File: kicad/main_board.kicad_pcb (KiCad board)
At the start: 2 copper layers, 42 x 67 mm, 66 parts, among them J1 Conn_01x18, J2 Conn_01x18, J3 Conn_01x07, J4 Conn_01x07, J5 Conn_01x07, J6 Conn_01x07, J7 Conn_01x07, J8 TYPE-C-31-M-12, J9 TYPE-C-31-M-12, Q1 DMG2301L-7, Q2 DMG2301L-7, Q3 DMG2301L-7, Q4 DMG2301L-7, Q5 DMG2301L-7, SW1 Reset, SW2 Boot, U1 XC6220B331MR, U2 RP2040, U3 W25Q128JVS, U4 COS724, U5 COS724, U6 USBLC6-2SC6, U7 USBLC6-2SC6, Y1 Crystal_GND24

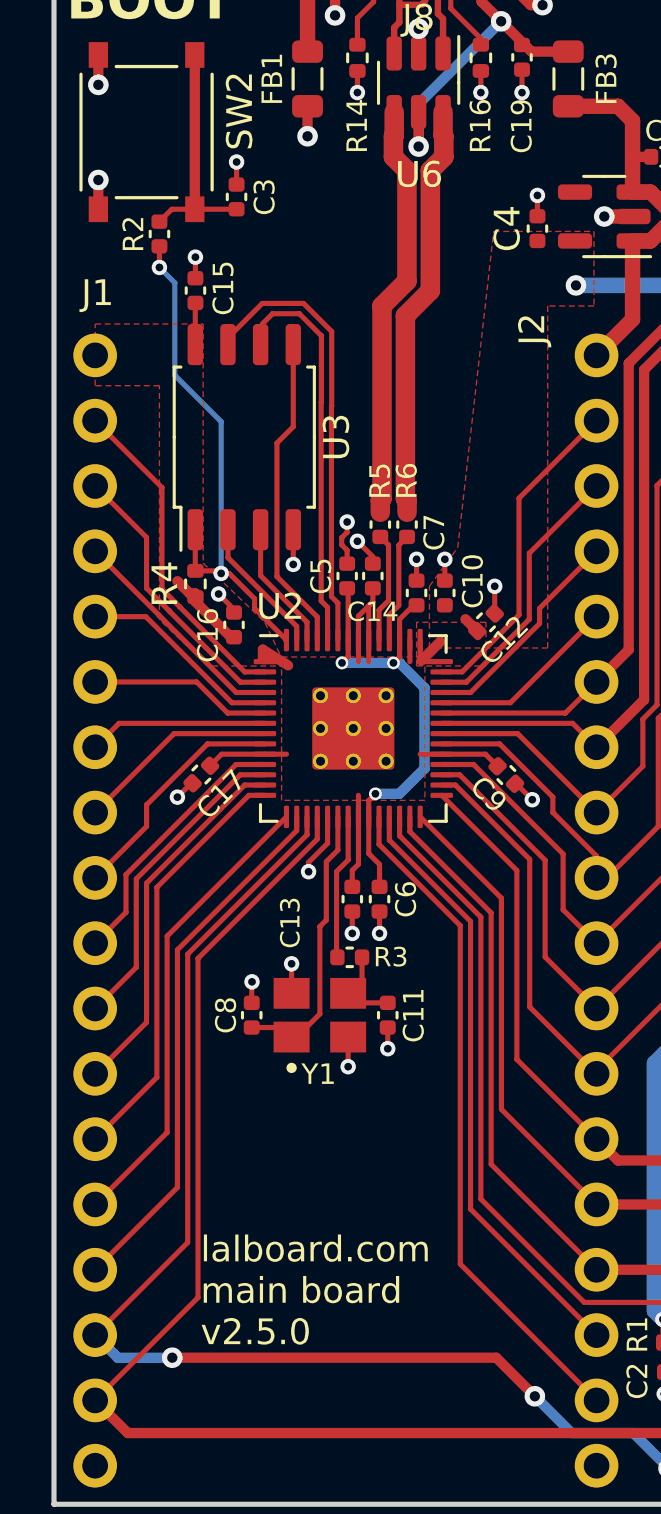
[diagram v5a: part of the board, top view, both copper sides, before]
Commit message: Main board v2.5.1
- Remove the decoupling capacitor on the boot selection button
- Fix the part selection in the BOM for the 27 ohm usb series resistors
(old part was mistakenly a 27kohm resistor)
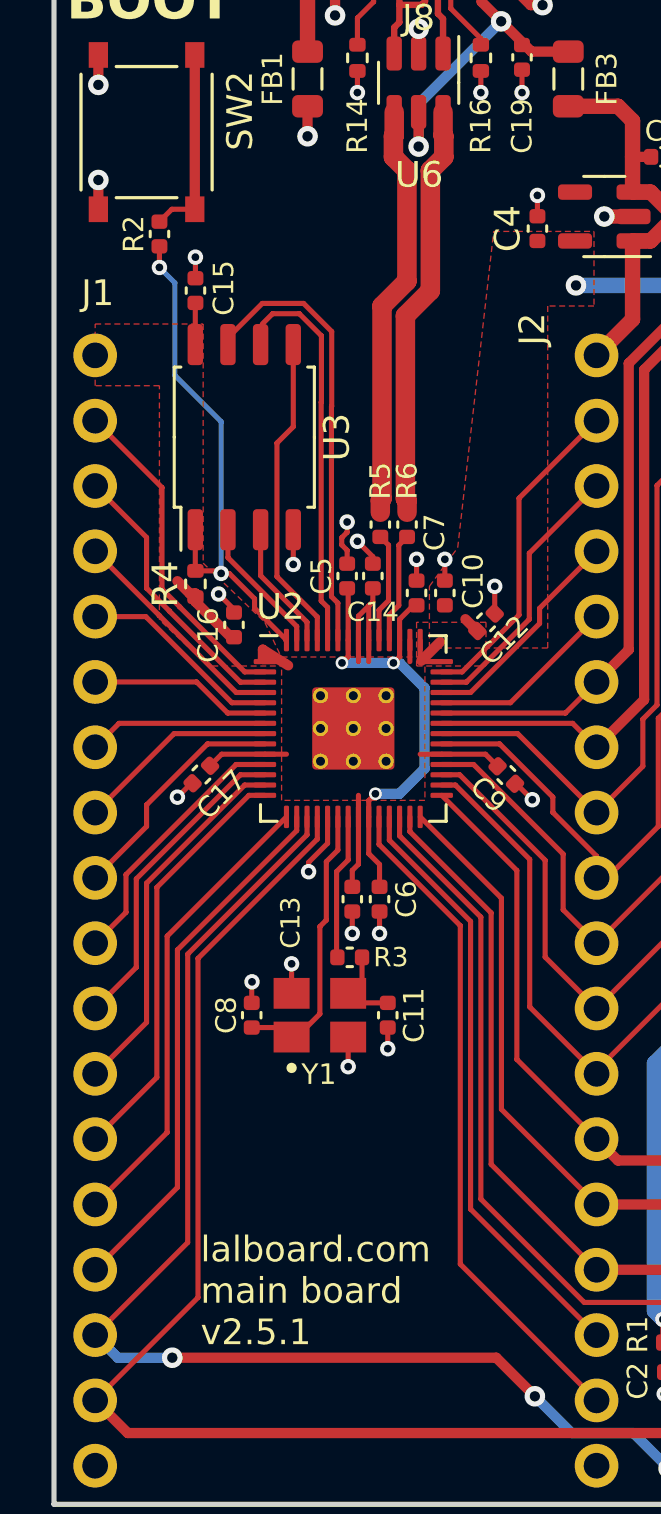
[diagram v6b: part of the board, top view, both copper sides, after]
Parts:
- removed C3: 100n, Capacitor_SMD:C_0402_1005Metric
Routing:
- net Net-(R2-Pad1): track 9.20 -> 7.57 mm
- net GND: track 50.4 -> 49.5 mm, vias 43 -> 42
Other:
- board text added: "lalboard.com main board v2.5.1"
- board text removed: "lalboard.com main board v2.5.0"
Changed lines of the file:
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@@
   (net 1 "GND")
   (net 2 "/RUN")
-  (net 3 "Net-(C3-Pad1)")
+  (net 3 "Net-(R2-Pad1)")
   (net 4 "+5V")
   (net 5 "Net-(U6-VBUS)")
@@
       (stroke (width 0.127) (type solid)) (layer "F.Fab"))
     (pad "1" smd rect (at -3 -1.875 270) (size 1 0.75) (layers "F.Cu" "F.Paste" "F.Mask")
-      (net 3 "Net-(C3-Pad1)") (pinfunction "1") (pintype "passive") (solder_mask_margin 0.102))
+      (net 3 "Net-(R2-Pad1)") (pinfunction "1") (pintype "passive") (solder_mask_margin 0.102))
     (pad "1" smd rect (at 3 -1.875 270) (size 1 0.75) (layers "F.Cu" "F.Paste" "F.Mask")
-      (net 3 "Net-(C3-Pad1)") (pinfunction "1") (pintype "passive") (solder_mask_margin 0.102))
+      (net 3 "Net-(R2-Pad1)") (pinfunction "1") (pintype "passive") (solder_mask_margin 0.102))
     (pad "2" smd rect (at -3 1.875 270) (size 1 0.75) (layers "F.Cu" "F.Paste" "F.Mask")
       (net 1 "GND") (pinfunction "2") (pintype "passive") (solder_mask_margin 0.102))
@@
     )
   )
-  (footprint "Capacitor_SMD:C_0402_1005Metric" (layer "F.Cu")
-    (at 157.1 49.1575 90)
-    (descr "Capacitor SMD 0402 (1005 Metric), square (rectangular) end terminal, IPC_7351 nominal, (Body size source: IPC-SM-782 page 76, https://www.pcb-3d.com/wordpress/wp-content/uploads/ipc-sm-782a_amendment_1_and_2.pdf), generated with kicad-footprint-generator")
-    (tags "capacitor")
-    (property "JLCPCB P/N" "C307331")
-    (property "Sheetfile" "main_board.kicad_sch")
-    (property "Sheetname" "")
-    (property "ki_description" "Unpolarized capacitor, small symbol")
-    (property "ki_keywords" "capacitor cap")
-    (attr smd)
-    (fp_text reference "C3" (at -0.000001 1.1 90) (layer "F.SilkS")
-        (effects (font (size 0.8 0.8) (thickness 0.15)))
-    )
-    (fp_text value "100n" (at 0 1.16 90) (layer "F.Fab")
-        (effects (font (size 1 1) (thickness 0.15)))
-    )
-    (fp_text user "${REFERENCE}" (at 0 0 90) (layer "F.Fab")
-        (effects (font (size 0.25 0.25) (thickness 0.04)))
-    )
-    (fp_line (start -0.107836 -0.36) (end 0.107836 -0.36)
-      (stroke (width 0.12) (type solid)) (layer "F.SilkS"))
-    (fp_line (start -0.107836 0.36) (end 0.107836 0.36)
-      (stroke (width 0.12) (type solid)) (layer "F.SilkS"))
-    (fp_line (start -0.91 -0.46) (end 0.91 -0.46)
-      (stroke (width 0.05) (type solid)) (layer "F.CrtYd"))
-    (fp_line (start -0.91 0.46) (end -0.91 -0.46)
-      (stroke (width 0.05) (type solid)) (layer "F.CrtYd"))
-    (fp_line (start 0.91 -0.46) (end 0.91 0.46)
-      (stroke (width 0.05) (type solid)) (layer "F.CrtYd"))
-    (fp_line (start 0.91 0.46) (end -0.91 0.46)
-      (stroke (width 0.05) (type solid)) (layer "F.CrtYd"))
-    (fp_line (start -0.5 -0.25) (end 0.5 -0.25)
-      (stroke (width 0.1) (type solid)) (layer "F.Fab"))
-    (fp_line (start -0.5 0.25) (end -0.5 -0.25)
-      (stroke (width 0.1) (type solid)) (layer "F.Fab"))
-    (fp_line (start 0.5 -0.25) (end 0.5 0.25)
-      (stroke (width 0.1) (type solid)) (layer "F.Fab"))
-    (fp_line (start 0.5 0.25) (end -0.5 0.25)
-      (stroke (width 0.1) (type solid)) (layer "F.Fab"))
-    (pad "1" smd roundrect (at -0.48 0 90) (size 0.56 0.62) (layers "F.Cu" "F.Paste" "F.Mask") (roundrect_rratio 0.25)
-      (net 3 "Net-(C3-Pad1)") (pintype "passive"))
-    (pad "2" smd roundrect (at 0.48 0 90) (size 0.56 0.62) (layers "F.Cu" "F.Paste" "F.Mask") (roundrect_rratio 0.25)
-      (net 1 "GND") (pintype "passive"))
-    (model "${KICAD6_3DMODEL_DIR}/Capacitor_SMD.3dshapes/C_0402_1005Metric.wrl"
-      (offset (xyz 0 0 0))
-      (scale (xyz 1 1 1))
-      (rotate (xyz 0 0 0))
-    )
-  )
   (footprint "Resistor_SMD:R_0402_1005Metric" (layer "F.Cu")
     (at 175.2 81.9425 -90)
@@
       (stroke (width 0.1) (type solid)) (layer "F.Fab"))
     (pad "1" smd roundrect (at -0.48 0 270) (size 0.56 0.62) (layers "F.Cu" "F.Paste" "F.Mask") (roundrect_rratio 0.25)
-      (net 3 "Net-(C3-Pad1)") (pintype "passive"))
+      (net 3 "Net-(R2-Pad1)") (pintype "passive"))
     (pad "2" smd roundrect (at 0.48 0 270) (size 0.56 0.62) (layers "F.Cu" "F.Paste" "F.Mask") (roundrect_rratio 0.25)
       (net 57 "/QSPI_SS") (pintype "passive"))
@@
     (property "Sheetfile" "main_board.kicad_sch")
     (property "Sheetname" "")
+    (property "exclude_from_bom" "")
     (property "ki_description" "Generic connector, single row, 01x07, script generated (kicad-library-utils/schlib/autogen/connector/)")
     (property "ki_keywords" "connector")
-    (attr through_hole)
+    (attr through_hole exclude_from_bom)
     (fp_text reference "J3" (at 4.5 2.81) (layer "F.SilkS")
         (effects (font (size 0.75 0.75) (thickness 0.15)))
@@
     (property "Sheetfile" "main_board.kicad_sch")
     (property "Sheetname" "")
+    (property "exclude_from_bom" "")
     (property "ki_description" "Generic connector, single row, 01x18, script generated (kicad-library-utils/schlib/autogen/connector/)")
     (property "ki_keywords" "connector")
-    (attr through_hole)
+    (attr through_hole exclude_from_bom)
     (fp_text reference "J1" (at 0.1 -2.42 180) (layer "F.SilkS")
         (effects (font (size 1 1) (thickness 0.15)))
@@
     (property "Sheetfile" "main_board.kicad_sch")
     (property "Sheetname" "")
+    (property "exclude_from_bom" "")
     (property "ki_description" "Generic connector, single row, 01x07, script generated (kicad-library-utils/schlib/autogen/connector/)")
     (property "ki_keywords" "connector")
-    (attr through_hole)
+    (attr through_hole exclude_from_bom)
     (fp_text reference "J7" (at 4.67 2.8) (layer "F.SilkS")
         (effects (font (size 0.75 0.75) (thickness 0.15)))
@@
     (property "Sheetfile" "main_board.kicad_sch")
     (property "Sheetname" "")
+    (property "exclude_from_bom" "")
     (property "ki_description" "Generic connector, single row, 01x07, script generated (kicad-library-utils/schlib/autogen/connector/)")
     (property "ki_keywords" "connector")
-    (attr through_hole)
+    (attr through_hole exclude_from_bom)
     (fp_text reference "J5" (at 4.5 2.8) (layer "F.SilkS")
         (effects (font (size 0.75 0.75) (thickness 0.15)))
@@
     (property "Sheetfile" "main_board.kicad_sch")
     (property "Sheetname" "")
+    (property "exclude_from_bom" "")
     (property "ki_description" "Generic connector, single row, 01x18, script generated (kicad-library-utils/schlib/autogen/connector/)")
     (property "ki_keywords" "connector")
-    (attr through_hole)
+    (attr through_hole exclude_from_bom)
     (fp_text reference "J2" (at -2.5 -1.02 90) (layer "F.SilkS")
         (effects (font (size 1 1) (thickness 0.15)))
@@
     (property "Sheetfile" "main_board.kicad_sch")
     (property "Sheetname" "")
+    (property "exclude_from_bom" "")
     (property "ki_description" "Generic connector, single row, 01x07, script generated (kicad-library-utils/schlib/autogen/connector/)")
     (property "ki_keywords" "connector")
-    (attr through_hole)
+    (attr through_hole exclude_from_bom)
     (fp_text reference "J4" (at 4.5 2.81) (layer "F.SilkS")
         (effects (font (size 0.75 0.75) (thickness 0.15)))
@@
     (property "Sheetfile" "main_board.kicad_sch")
     (property "Sheetname" "")
+    (property "exclude_from_bom" "")
     (property "ki_description" "Generic connector, single row, 01x07, script generated (kicad-library-utils/schlib/autogen/connector/)")
     (property "ki_keywords" "connector")
-    (attr through_hole)
+    (attr through_hole exclude_from_bom)
     (fp_text reference "J6" (at 4.5 2.8) (layer "F.SilkS")
         (effects (font (size 0.75 0.75) (thickness 0.15)))
@@
     (effects (font (size 1.5 1.5) (thickness 0.25) bold) (justify left bottom))
   )
-  (gr_text "lalboard.com\nmain board\nv2.5.0" (at 155.7 91.7) (layer "F.SilkS")
+  (gr_text "lalboard.com\nmain board\nv2.5.1" (at 155.7 91.7) (layer "F.SilkS")
     (effects (font (size 1 1) (thickness 0.125)) (justify left))
   )
@@
   (segment (start 161.6 76.947939) (end 161.6 77.8) (width 0.2) (layer "F.Cu") (net 1))
   (segment (start 161.19 62.69) (end 161.4 62.9) (width 0.2) (layer "F.Cu") (net 1))
-  (segment (start 157.1 48.6775) (end 157.1 47.8) (width 0.2) (layer "F.Cu") (net 1))
   (segment (start 161.4 62.2) (end 161.19 62.41) (width 0.2) (layer "F.Cu") (net 1))
   (segment (start 159.24 80.13) (end 159.24 78.982061) (width 0.2) (layer "F.Cu") (net 1))
@@
   (via (at 180.2 45.1) (size 0.6) (drill 0.3) (layers "F.Cu" "B.Cu") (free) (net 1))
   (via (at 164.18 42.62) (size 0.8) (drill 0.4) (layers "F.Cu" "B.Cu") (net 1))
-  (via (at 157.1 47.8) (size 0.6) (drill 0.3) (layers "F.Cu" "B.Cu") (free) (net 1))
   (via (at 160.93 42.1) (size 0.8) (drill 0.4) (layers "F.Cu" "B.Cu") (net 1))
   (via (at 178.85 89.5) (size 0.8) (drill 0.4) (layers "F.Cu" "B.Cu") (free) (net 1))
@@
   (segment (start 155.475 49.6375) (end 154.5825 49.6375) (width 0.2) (layer "F.Cu") (net 3))
   (segment (start 155.475 49.6375) (end 155.475 43.6375) (width 0.4) (layer "F.Cu") (net 3))
-  (segment (start 155.475 49.6375) (end 157.1 49.6375) (width 0.2) (layer "F.Cu") (net 3))
   (segment (start 154.5825 49.6375) (end 154.1 50.12) (width 0.2) (layer "F.Cu") (net 3))
   (segment (start 173.2 48.97) (end 173.9 49.67) (width 0.6) (layer "F.Cu") (net 4))
